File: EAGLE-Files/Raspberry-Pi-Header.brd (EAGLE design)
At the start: 22.8 x 68.2 mm, 6 parts

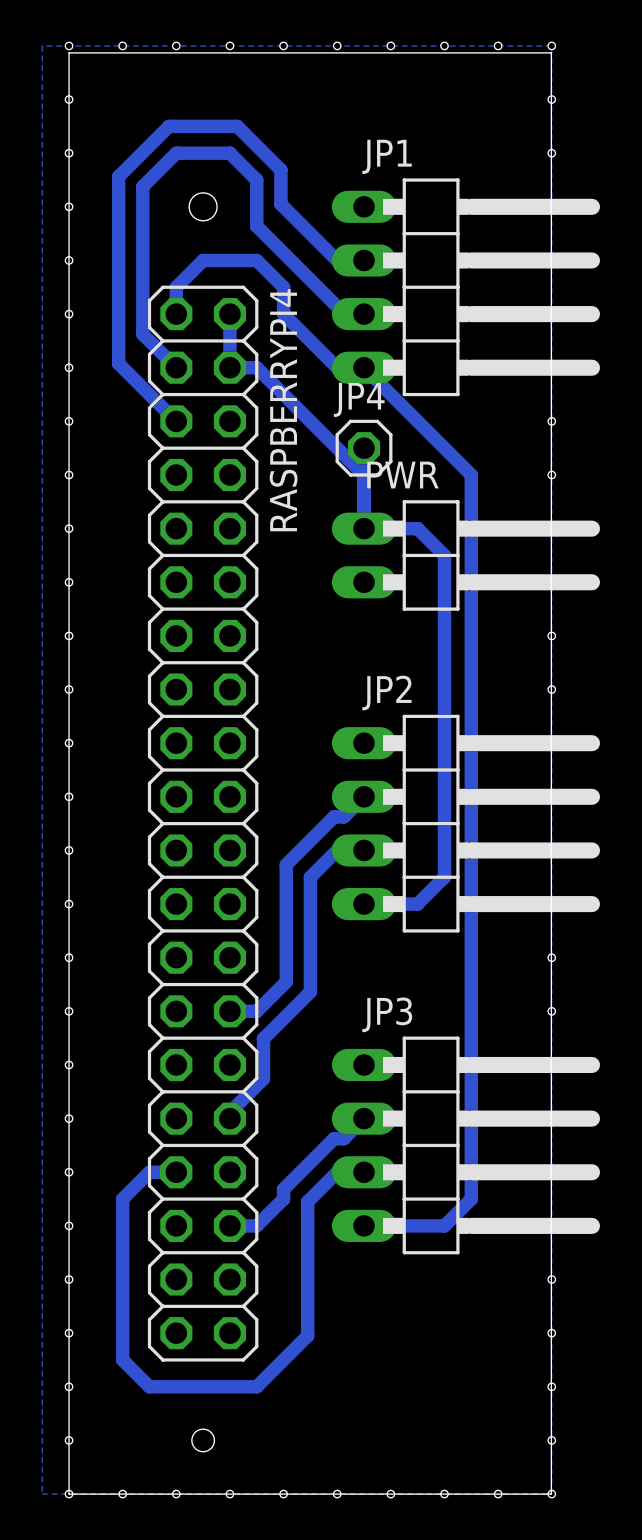
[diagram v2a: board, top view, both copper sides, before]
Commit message: Updated all boards for JLCPCB order
Also added the controller boards and schematics back
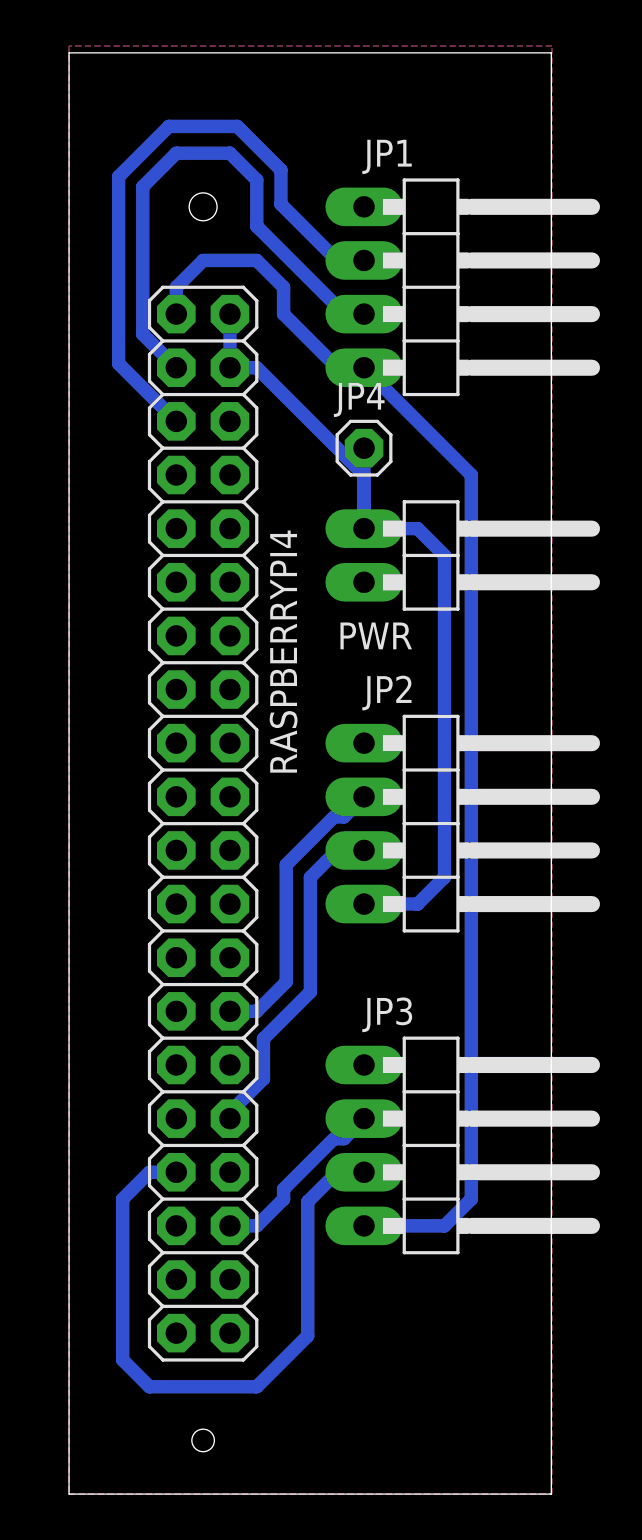
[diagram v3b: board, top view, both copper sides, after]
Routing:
- added copper zone on layer 1, net GND
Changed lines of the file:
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@@
 <wire x1="22.84" y1="68.25" x2="0" y2="68.25" width="0" layer="20"/>
 <wire x1="0" y1="68.25" x2="0" y2="0" width="0" layer="20"/>
-<dimension x1="-2.54" y1="60.96" x2="-2.54" y2="2.54" x3="-3.81" y3="31.75" textsize="1.778" layer="1"/>
 <hole x="6.35" y="2.54" drill="1.0668"/>
 <hole x="6.35" y="60.96" drill="1.3208"/>
-<dimension x1="0" y1="69.85" x2="22.86" y2="69.85" x3="11.43" y3="73.66" textsize="1.778" layer="1"/>
-<dimension x1="-2.54" y1="68.58" x2="-2.54" y2="0" x3="-8.89" y3="34.29" textsize="1.778" layer="1"/>
-<hole x="0" y="68.58" drill="0.35"/>
-<hole x="2.54" y="68.58" drill="0.35"/>
-<hole x="5.08" y="68.58" drill="0.35"/>
-<hole x="7.62" y="68.58" drill="0.35"/>
-<hole x="10.16" y="68.58" drill="0.35"/>
-<hole x="12.7" y="68.58" drill="0.35"/>
-<hole x="15.24" y="68.58" drill="0.35"/>
-<hole x="17.78" y="68.58" drill="0.35"/>
-<hole x="20.32" y="68.58" drill="0.35"/>
-<hole x="22.86" y="68.58" drill="0.35"/>
-<hole x="0" y="66.04" drill="0.35"/>
-<hole x="0" y="63.5" drill="0.35"/>
-<hole x="0" y="60.96" drill="0.35"/>
-<hole x="0" y="58.42" drill="0.35"/>
-<hole x="0" y="55.88" drill="0.35"/>
-<hole x="0" y="53.34" drill="0.35"/>
-<hole x="0" y="50.8" drill="0.35"/>
-<hole x="0" y="48.26" drill="0.35"/>
-<hole x="0" y="45.72" drill="0.35"/>
-<hole x="0" y="43.18" drill="0.35"/>
-<hole x="0" y="40.64" drill="0.35"/>
-<hole x="0" y="38.1" drill="0.35"/>
-<hole x="0" y="35.56" drill="0.35"/>
-<hole x="0" y="33.02" drill="0.35"/>
-<hole x="0" y="30.48" drill="0.35"/>
-<hole x="0" y="27.94" drill="0.35"/>
-<hole x="0" y="25.4" drill="0.35"/>
-<hole x="0" y="22.86" drill="0.35"/>
-<hole x="0" y="20.32" drill="0.35"/>
-<hole x="0" y="17.78" drill="0.35"/>
-<hole x="0" y="15.24" drill="0.35"/>
-<hole x="0" y="12.7" drill="0.35"/>
-<hole x="0" y="10.16" drill="0.35"/>
-<hole x="0" y="7.62" drill="0.35"/>
-<hole x="0" y="5.08" drill="0.35"/>
-<hole x="0" y="2.54" drill="0.35"/>
-<hole x="0" y="0" drill="0.35"/>
-<hole x="2.54" y="0" drill="0.35"/>
-<hole x="5.08" y="0" drill="0.35"/>
-<hole x="7.62" y="0" drill="0.35"/>
-<hole x="10.16" y="0" drill="0.35"/>
-<hole x="12.7" y="0" drill="0.35"/>
-<hole x="15.24" y="0" drill="0.35"/>
-<hole x="17.78" y="0" drill="0.35"/>
-<hole x="20.32" y="0" drill="0.35"/>
-<hole x="22.86" y="0" drill="0.35"/>
-<hole x="22.86" y="66.04" drill="0.35"/>
-<hole x="22.86" y="63.5" drill="0.35"/>
-<hole x="22.86" y="60.96" drill="0.35"/>
-<hole x="22.86" y="58.42" drill="0.35"/>
-<hole x="22.86" y="55.88" drill="0.35"/>
-<hole x="22.86" y="53.34" drill="0.35"/>
-<hole x="22.86" y="50.8" drill="0.35"/>
-<hole x="22.86" y="48.26" drill="0.35"/>
-<hole x="22.86" y="45.72" drill="0.35"/>
-<hole x="22.86" y="43.18" drill="0.35"/>
-<hole x="22.86" y="40.64" drill="0.35"/>
-<hole x="22.86" y="38.1" drill="0.35"/>
-<hole x="22.86" y="35.56" drill="0.35"/>
-<hole x="22.86" y="33.02" drill="0.35"/>
-<hole x="22.86" y="30.48" drill="0.35"/>
-<hole x="22.86" y="27.94" drill="0.35"/>
-<hole x="22.86" y="25.4" drill="0.35"/>
-<hole x="22.86" y="22.86" drill="0.35"/>
-<hole x="22.86" y="20.32" drill="0.35"/>
-<hole x="22.86" y="17.78" drill="0.35"/>
-<hole x="22.86" y="15.24" drill="0.35"/>
-<hole x="22.86" y="12.7" drill="0.35"/>
-<hole x="22.86" y="10.16" drill="0.35"/>
-<hole x="22.86" y="7.62" drill="0.35"/>
-<hole x="22.86" y="5.08" drill="0.35"/>
-<hole x="22.86" y="2.54" drill="0.35"/>
 </plain>
 <attributes>
@@
 </class>
 </classes>
-<designrules name="default2 *">
-<description language="de">&lt;b&gt;EAGLE Design Rules&lt;/b&gt;
-&lt;p&gt;
-Die Standard-Design-Rules sind so gewählt, dass sie für
-die meisten Anwendungen passen. Sollte ihre Platine
-besondere Anforderungen haben, treffen Sie die erforderlichen
-Einstellungen hier und speichern die Design Rules unter
-einem neuen Namen ab.</description>
-<description language="en">&lt;b&gt;EAGLE Design Rules&lt;/b&gt;
-&lt;p&gt;
-The default Design Rules have been set to cover
-a wide range of applications. Your particular design
-may have different requirements, so please make the
-necessary adjustments and save your customized
-design rules under a new name.</description>
+<designrules name="jlcpcb-2layers">
+<description language="en">&lt;b&gt;JLCPCB design rules (2 layers)&lt;/b&gt;
+&lt;ul&gt;
+&lt;li&gt;Board thickness: 1.6mm&lt;/li&gt;
+&lt;li&gt;Copper weight: 1oz (35um)&lt;/li&gt;
+&lt;li&gt;Note: annular ring aren't minimal&lt;/li&gt;
+&lt;/ul&gt;</description>
 <param name="layerSetup" value="(1*16)"/>
 <param name="mtCopper" value="0.035mm 0.035mm 0.035mm 0.035mm 0.035mm 0.035mm 0.035mm 0.035mm 0.035mm 0.035mm 0.035mm 0.035mm 0.035mm 0.035mm 0.035mm 0.035mm"/>
-<param name="mtIsolate" value="1.5mm 0.15mm 0.2mm 0.15mm 0.2mm 0.15mm 0.2mm 0.15mm 0.2mm 0.15mm 0.2mm 0.15mm 0.2mm 0.15mm 0.2mm"/>
-<param name="mdWireWire" value="20mil"/>
-<param name="mdWirePad" value="20mil"/>
-<param name="mdWireVia" value="20mil"/>
-<param name="mdPadPad" value="20mil"/>
-<param name="mdPadVia" value="20mil"/>
-<param name="mdViaVia" value="20mil"/>
-<param name="mdSmdPad" value="20mil"/>
-<param name="mdSmdVia" value="20mil"/>
-<param name="mdSmdSmd" value="20mil"/>
+<param name="mtIsolate" value="1.6mm 0.15mm 0.2mm 0.15mm 0.2mm 0.15mm 0.2mm 0.15mm 0.2mm 0.15mm 0.2mm 0.15mm 0.2mm 0.15mm 0.2mm"/>
+<param name="mdWireWire" value="5mil"/>
+<param name="mdWirePad" value="5mil"/>
+<param name="mdWireVia" value="5mil"/>
+<param name="mdPadPad" value="5mil"/>
+<param name="mdPadVia" value="5mil"/>
+<param name="mdViaVia" value="5mil"/>
+<param name="mdSmdPad" value="5mil"/>
+<param name="mdSmdVia" value="5mil"/>
+<param name="mdSmdSmd" value="5mil"/>
 <param name="mdViaViaSameLayer" value="6mil"/>
 <param name="mnLayersViaInSmd" value="2"/>
-<param name="mdCopperDimension" value="40mil"/>
+<param name="mdCopperDimension" value="0.2mm"/>
 <param name="mdDrill" value="6mil"/>
 <param name="mdSmdStop" value="0mil"/>
-<param name="msWidth" value="25mil"/>
-<param name="msDrill" value="0.45mm"/>
-<param name="msMicroVia" value="9.99mm"/>
+<param name="msWidth" value="5mil"/>
+<param name="msDrill" value="0.3mm"/>
+<param name="msMicroVia" value="0.3mm"/>
 <param name="msBlindViaRatio" value="0.5"/>
-<param name="rvPadTop" value="0.25"/>
-<param name="rvPadInner" value="0.25"/>
-<param name="rvPadBottom" value="0.25"/>
-<param name="rvViaOuter" value="0.25"/>
-<param name="rvViaInner" value="0.25"/>
-<param name="rvMicroViaOuter" value="0.25"/>
-<param name="rvMicroViaInner" value="0.25"/>
+<param name="rvPadTop" value="0.4"/>
+<param name="rvPadInner" value="0"/>
+<param name="rvPadBottom" value="0.4"/>
+<param name="rvViaOuter" value="0"/>
+<param name="rvViaInner" value="0"/>
+<param name="rvMicroViaOuter" value="0"/>
+<param name="rvMicroViaInner" value="0"/>
 <param name="rlMinPadTop" value="10mil"/>
-<param name="rlMaxPadTop" value="20mil"/>
+<param name="rlMaxPadTop" value="80mil"/>
 <param name="rlMinPadInner" value="10mil"/>
 <param name="rlMaxPadInner" value="20mil"/>
 <param name="rlMinPadBottom" value="10mil"/>
-<param name="rlMaxPadBottom" value="20mil"/>
-<param name="rlMinViaOuter" value="8mil"/>
+<param name="rlMaxPadBottom" value="80mil"/>
+<param name="rlMinViaOuter" value="3mil"/>
 <param name="rlMaxViaOuter" value="20mil"/>
 <param name="rlMinViaInner" value="8mil"/>
 <param name="rlMaxViaInner" value="20mil"/>
-<param name="rlMinMicroViaOuter" value="4mil"/>
+<param name="rlMinMicroViaOuter" value="3mil"/>
 <param name="rlMaxMicroViaOuter" value="20mil"/>
 <param name="rlMinMicroViaInner" value="4mil"/>
@@
 <param name="srMinRoundness" value="0mil"/>
 <param name="srMaxRoundness" value="0mil"/>
-<param name="slThermalIsolate" value="20mil"/>
+<param name="slThermalIsolate" value="10mil"/>
 <param name="slThermalsForVias" value="0"/>
 <param name="dpMaxLengthDifference" value="10mm"/>
@@
 <elements>
 <element name="RASPBERRYPI4" library="pinhead" library_urn="urn:adsk.eagle:library:325" package="2X20" package3d_urn="urn:adsk.eagle:package:22443/2" value="" x="6.35" y="31.75" smashed="yes" rot="R270">
-<attribute name="NAME" x="9.525" y="57.15" size="1.27" layer="25" ratio="10" rot="R270"/>
+<attribute name="NAME" x="9.525" y="45.72" size="1.27" layer="25" ratio="10" rot="R270"/>
 <attribute name="POPULARITY" value="12" x="-10.16" y="-7.62" size="1.778" layer="27" rot="R270" display="off"/>
 <attribute name="VALUE" x="1.905" y="57.15" size="1.27" layer="27" rot="R270"/>
 </element>
 <element name="PWR" library="pinhead" library_urn="urn:adsk.eagle:library:325" package="1X02/90" package3d_urn="urn:adsk.eagle:package:22437/2" value="" x="17.78" y="44.45" smashed="yes" rot="R270">
-<attribute name="NAME" x="13.97" y="47.625" size="1.27" layer="25" ratio="10"/>
+<attribute name="NAME" x="12.7" y="40.005" size="1.27" layer="25" ratio="10"/>
 <attribute name="POPULARITY" value="24" x="17.78" y="44.45" size="1.778" layer="27" rot="R270" display="off"/>
 <attribute name="VALUE" x="13.97" y="40.005" size="1.27" layer="27"/>
@@
 <contactref element="RASPBERRYPI4" pad="14"/>
 <polygon width="0.1524" layer="16">
-<vertex x="-1.27" y="68.58"/>
-<vertex x="-1.27" y="0"/>
+<vertex x="0" y="68.58"/>
+<vertex x="0" y="0"/>
 <vertex x="22.86" y="0"/>
 <vertex x="22.86" y="68.58"/>
@@
 <contactref element="JP2" pad="1"/>
 <contactref element="JP1" pad="1"/>
-<wire x1="7.62" y1="15.24" x2="7.62" y2="20.32" width="0" layer="19" extent="1-1"/>
-<wire x1="5.08" y1="25.4" x2="7.62" y2="20.32" width="0" layer="19" extent="1-1"/>
-<wire x1="7.62" y1="40.64" x2="5.08" y2="45.72" width="0" layer="19" extent="1-1"/>
-<wire x1="5.08" y1="7.62" x2="7.62" y2="15.24" width="0" layer="19" extent="1-1"/>
+<polygon width="0.1524" layer="1">
+<vertex x="0" y="68.58"/>
+<vertex x="0" y="0"/>
+<vertex x="22.86" y="0"/>
+<vertex x="22.86" y="68.58"/>
+</polygon>
 </signal>
 <signal name="+3V3">
